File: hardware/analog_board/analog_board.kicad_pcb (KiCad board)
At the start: 4 copper layers, 135 x 115 mm, 334 parts, among them J1 2x5 牛角座, J2 Conn_02x08_Counter_Clockwise, J3 Conn_01x04_Pin, J4 Conn_01x08, J5 CH1, J6 CH1, J7 CH1, Q1 MMBT3906, Q2 MMBT3906, U1 GW2A-LV18EQ144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

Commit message: feat：添加平衡铜
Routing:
- net +1V0: track 89.9 -> 56.7 mm
- net +3.3V: track 59.4 -> 45.7 mm, vias 19 -> 16
- net GND: track 142.6 -> 142.1 mm, vias 478 -> 484
- net +7V: vias 3 -> 2
- net +5VA: vias 13 -> 7
- added copper zone on In2.Cu, net GND

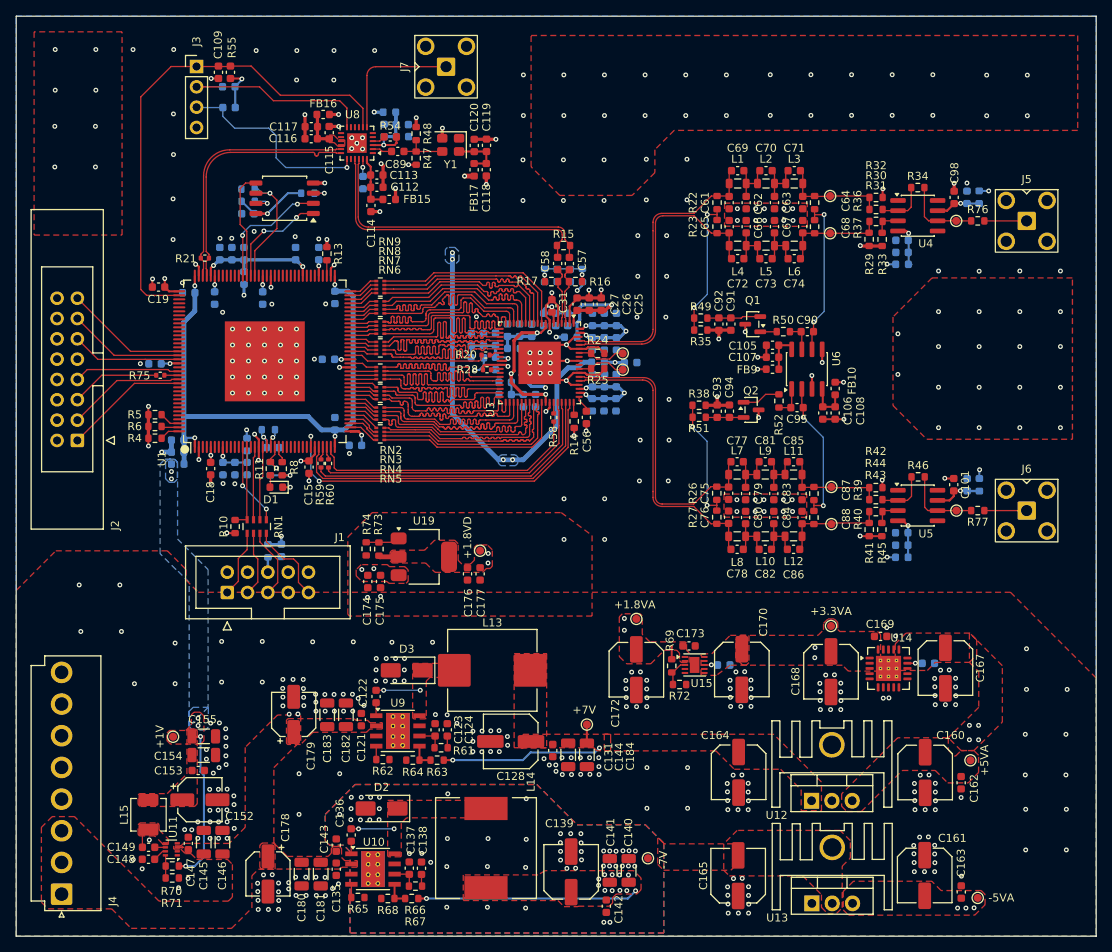
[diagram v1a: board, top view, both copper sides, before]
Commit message: feat：DCDC移至控制板
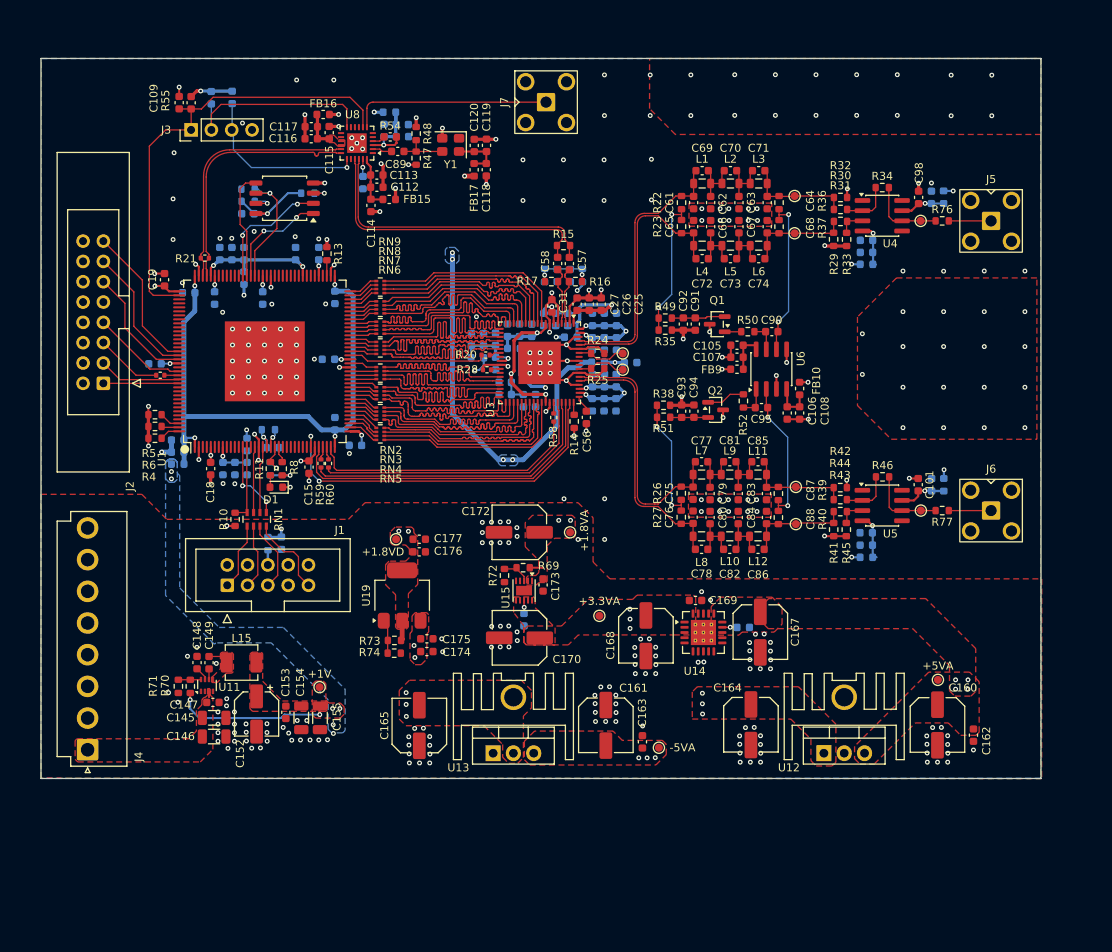
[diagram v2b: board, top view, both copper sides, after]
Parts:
- removed C121, C122, C131, C135, C136, C142: 100nF, Capacitor_SMD:C_0603_1608Metric
- removed C123: 330pF, Capacitor_SMD:C_0603_1608Metric
- removed C124: 33nF, Capacitor_SMD:C_0603_1608Metric
- removed C128, C139: 100uF, Capacitor_SMD:C_Elec_6.3x7.7
- removed C137: 1.2nF, Capacitor_SMD:C_0603_1608Metric
- removed C138: 2.2uF, Capacitor_SMD:C_0603_1608Metric
- removed C140, C141, C144, C184: 22uF, Capacitor_SMD:C_1206_3216Metric
- removed C143: 1uF, Capacitor_SMD:C_0603_1608Metric
- removed C178, C179: 22uF, Capacitor_SMD:CP_Elec_5x5.4
- removed C180, C181, C182, C183: 1uF, Capacitor_SMD:C_1206_3216Metric
- removed D2, D3: SS34, Diode_SMD:D_SMA
- removed L13: 33uH, Inductor_SMD:L_Changjiang_FXL1040
- removed L14: 150uH, Inductor_SMD:L_12x12mm_H6mm
- removed R61: 1.6kR, Resistor_SMD:R_0603_1608Metric
- removed R62: 196kR, Resistor_SMD:R_0603_1608Metric
- removed R63: 77.5k, Resistor_SMD:R_0603_1608Metric
- removed R64, R68: 10kR, Resistor_SMD:R_0603_1608Metric
- removed R65: 237kR, Resistor_SMD:R_0603_1608Metric
- removed R66: 3.3kR, Resistor_SMD:R_0603_1608Metric
- removed R67: 77.5kR, Resistor_SMD:R_0603_1608Metric
- removed TP10: -7V, TestPoint:TestPoint_Pad_D1.0mm
- removed TP9: +7V, TestPoint:TestPoint_Pad_D1.0mm
- removed U10, U9: TPS54360DDA, Package_SO:TI_SO-PowerPAD-8_ThermalVias
- moved HS4 44.1 mm to (86.5, 120.1)
- moved C161 44.1 mm to (100.7, 114.9)
- moved C163 44.1 mm to (105.3, 117.0)
- moved C165 44.1 mm to (77.4, 115.0)
- moved TP14 44.1 mm to (107.3, 117.7)
- moved U13 44.1 mm to (86.6, 118.4)
- moved TP16 29.0 mm to (99.9, 101.2)
- moved C170 28.1 mm to (89.9, 104.0), turned to 180 degrees
- moved R72 25.8 mm to (88.0, 96.2), turned to 90 degrees
- moved C171 25.6 mm to (90.5, 101.7), turned to 90 degrees
- moved C148 25.3 mm to (49.6, 107.1), turned to 90 degrees
- moved C149 24.3 mm to (51.1, 107.1), turned to -90 degrees
- moved R71 24.0 mm to (47.3, 110.1), turned to 90 degrees
- moved C166 23.6 mm to (117.9, 102.7)
- moved C167 23.6 mm to (120.0, 103.3)
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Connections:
- J4 pad 3: +17V -> -17V
- J4 pad 4: -17V -> +7V
- J4 pad 6: -17V -> -7V
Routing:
- net GND: track 142.1 -> 115.0 mm, vias 484 -> 311
- net +7V: track 22.4 -> 0.00 mm, vias 2 -> 3
- net Clock_V_{DD}: track 46.8 -> 55.7 mm
- net /Clock/10MHz_OUT: track 16.9 -> 25.2 mm
- net /FPGA_Ctrl.Ctrl_SPI_CS: track 15.7 -> 9.48 mm
- net /Clock/RESET_N: track 63.2 -> 57.2 mm
- net Net-(D3-K): track 5.51 -> 0.00 mm, vias 2 -> 0
- net Net-(D2-K): track 5.37 -> 0.00 mm, vias 2 -> 0
- net /DAC/IOUT2_N: track 37.7 -> 33.2 mm
- net /DAC/IOUT2_P: track 37.7 -> 33.2 mm
- net /FPGA_Ctrl.Ctrl_SPI_CLK: track 14.8 -> 10.4 mm
- net /DAC/IOUT1_N: track 37.9 -> 33.7 mm
- net /DAC/IOUT1_P: track 37.8 -> 33.7 mm
- net Net-(U9-COMP): track 3.46 -> 0.00 mm
- net Net-(U10-COMP): track 3.35 -> 0.00 mm
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- added copper zone on In2.Cu, net +7V
- removed copper zone on In2.Cu, net -17V
- removed copper zone on B.Cu, net -7V
- removed copper zone on F.Cu, net Net-(D2-K)
- removed copper zone on F.Cu, net Net-(D3-K)
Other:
- board size 135 x 115 mm -> 125 x 90 mm

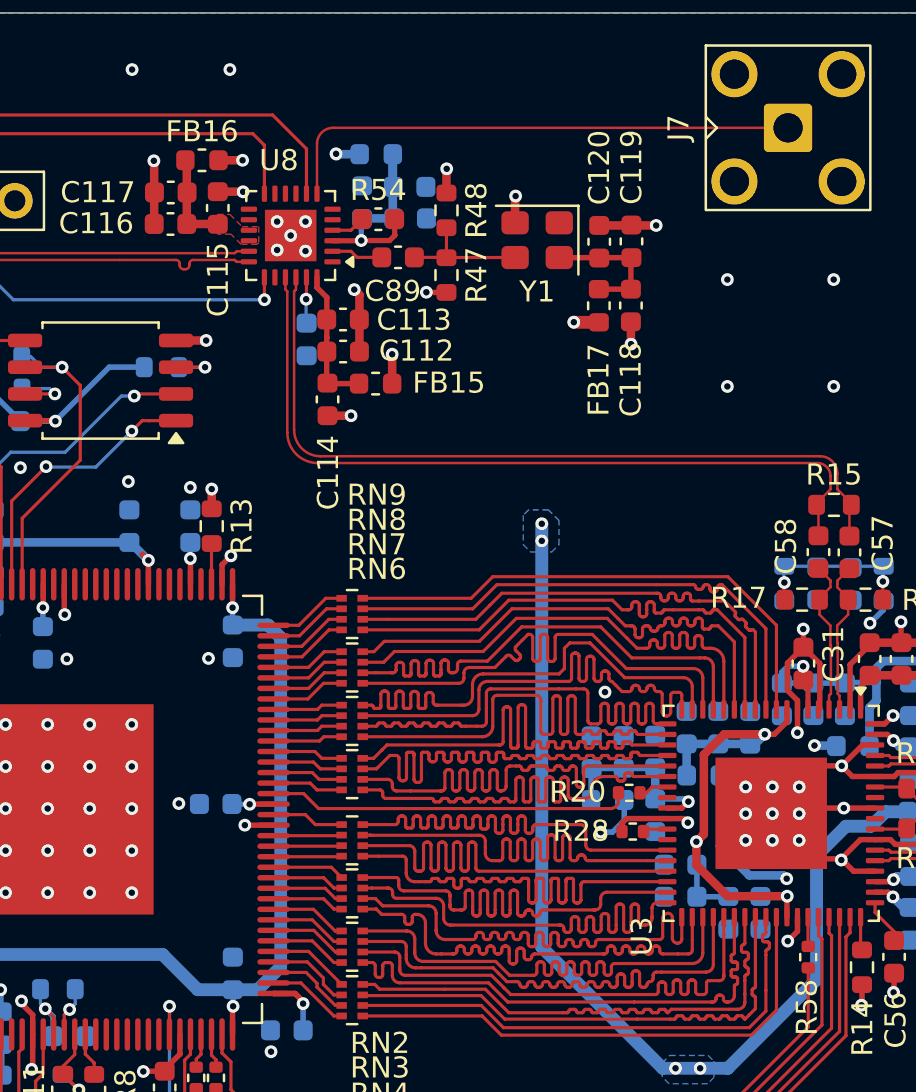
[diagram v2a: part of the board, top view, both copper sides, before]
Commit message: debug：输出10MHz时钟线宽修正为5.96mm(50Ω)
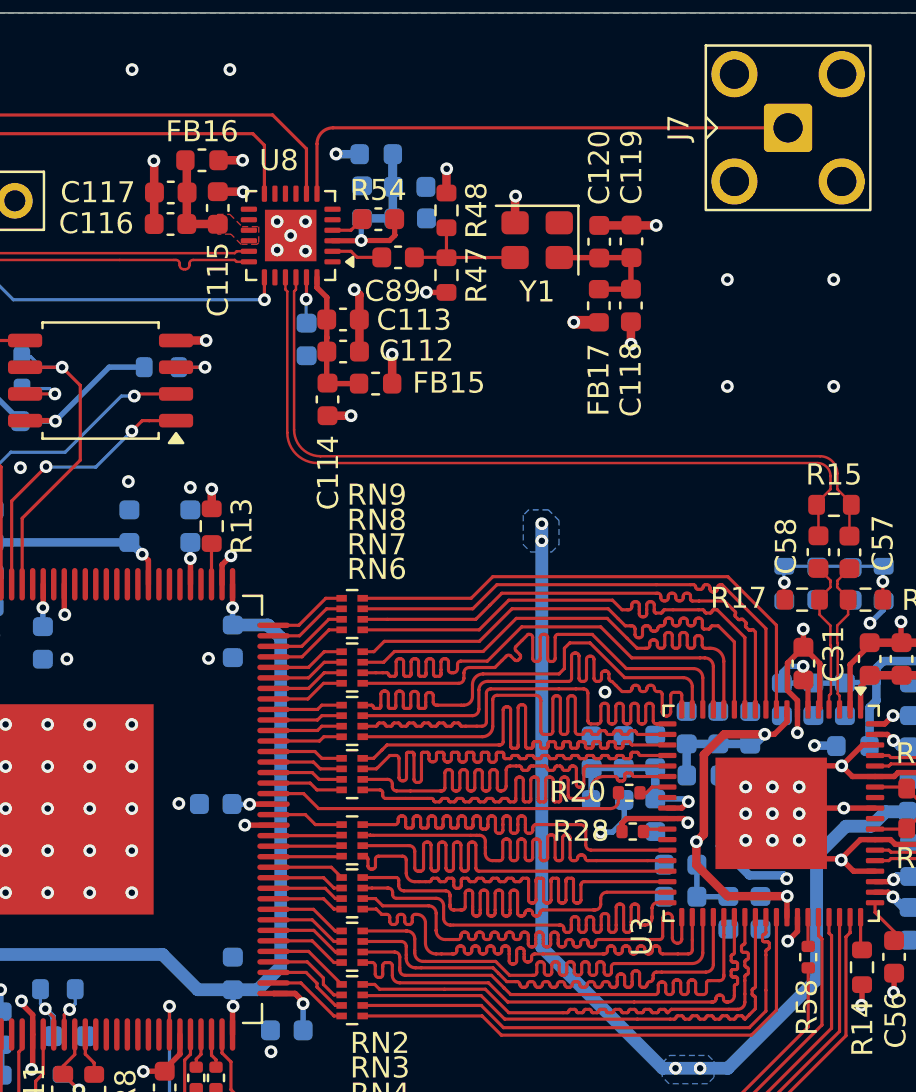
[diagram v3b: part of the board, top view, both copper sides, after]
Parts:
- U2: value W25Q32JVSS -> GD25Q32JVSS
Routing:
- net /DAC/P1D9: track 25.2 -> 26.3 mm
- net /DAC/P2D12: track 25.4 -> 26.5 mm
- net /DAC/P2D8: track 25.1 -> 26.1 mm
- net /DAC/P2D9: track 25.1 -> 25.8 mm
